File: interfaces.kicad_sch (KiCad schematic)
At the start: 10 parts, among them J13 JST_SH_1x4_SM04B-SRSS-TB-LF-SN, J14 JST_SH_1x4_SM04B-SRSS-TB-LF-SN, U7 MAX3051EKA

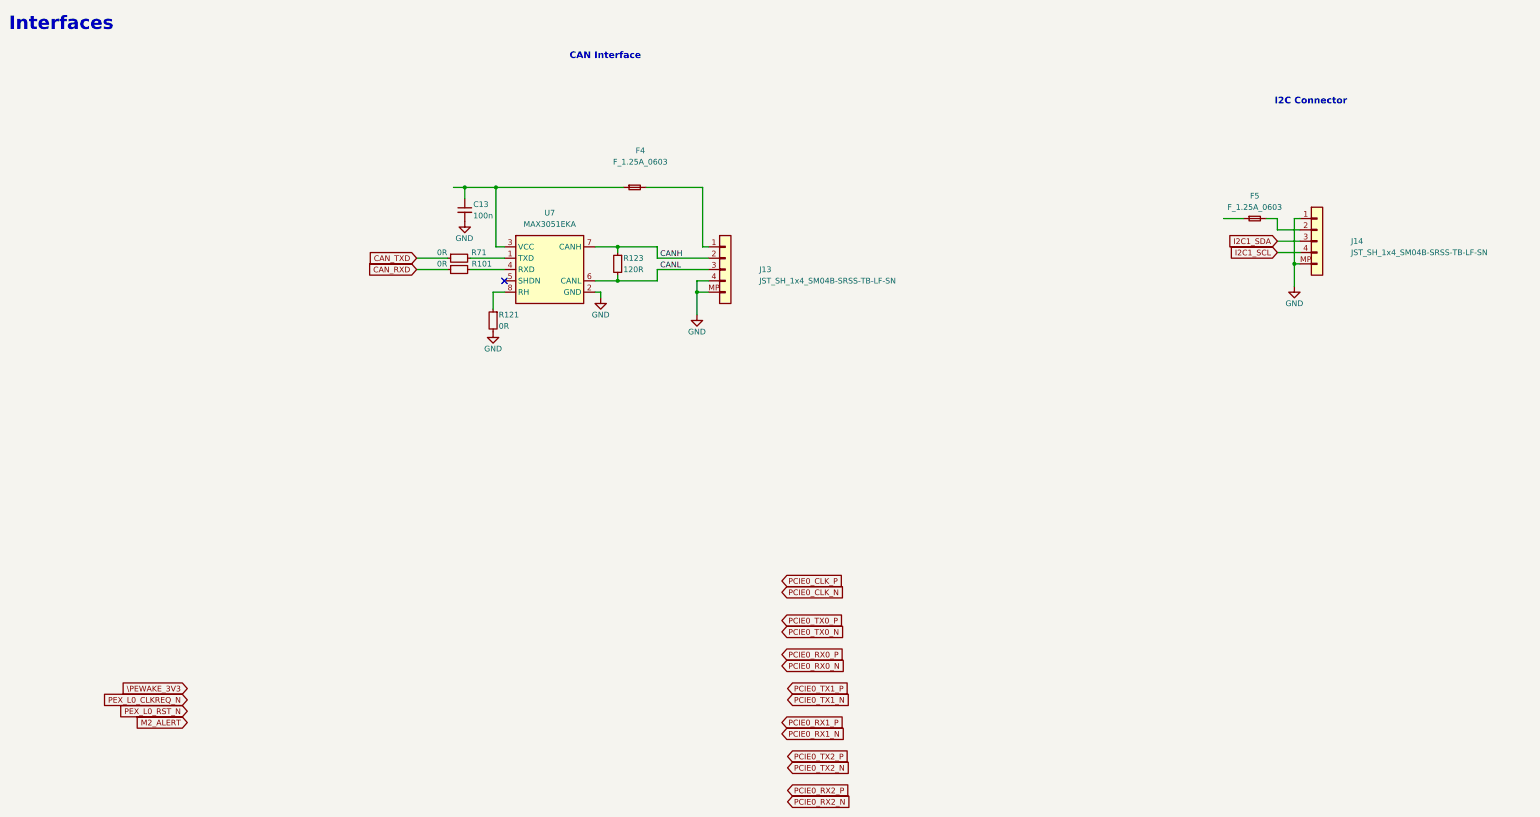
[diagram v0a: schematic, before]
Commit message: fix(schematic): remediate camera clocking, power sequencing, and ERC errors
- Connect Sony IMX219 master clocks (CAM0/1_MCLK) from SoM pins 116/122
- Connect independent PWDN hardware resets from SoM pins 114/120
- Isolate sensor I2C channels (CAM0/1_SCL/SDA) downstream of PCA9547
- Upgrade U11 digital core LDO to TLV75512PDBVR (500mA rating)
- Ground R132 to enable serial EEPROM write-protect
- Connect 3V3_SYS power rail to CAN transceiver U7 and fuse F5
- Eliminate dangling global labels across all sheets
- Configure 25 mil connection grid and achieve 0 ERC errors
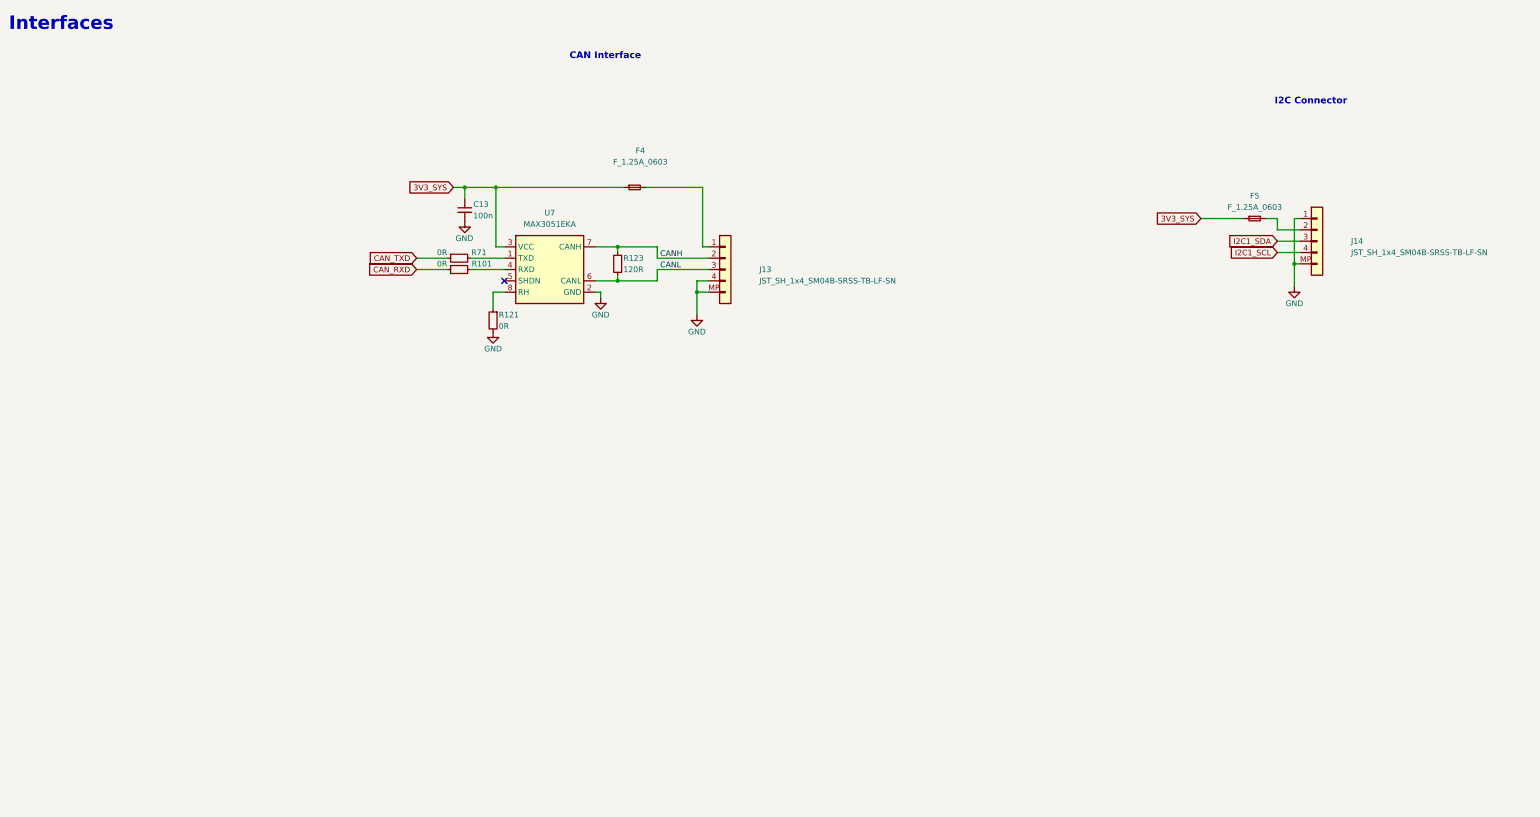
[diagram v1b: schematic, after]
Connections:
- net 3V3_SYS: now reaches C13.1, F4.1, U7.3 (VCC)
- net 3V3_SYS: now also F5.1

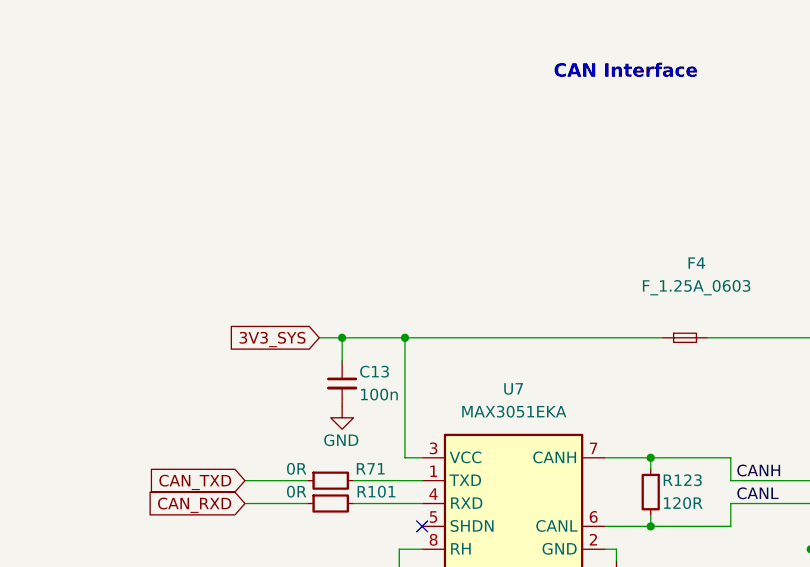
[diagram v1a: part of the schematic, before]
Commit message: fix(display, interfaces): connect U7 VCC to 3V3_SYS, change IC6 VCCA to 1V8_SYS, add display PWR_FLAGs
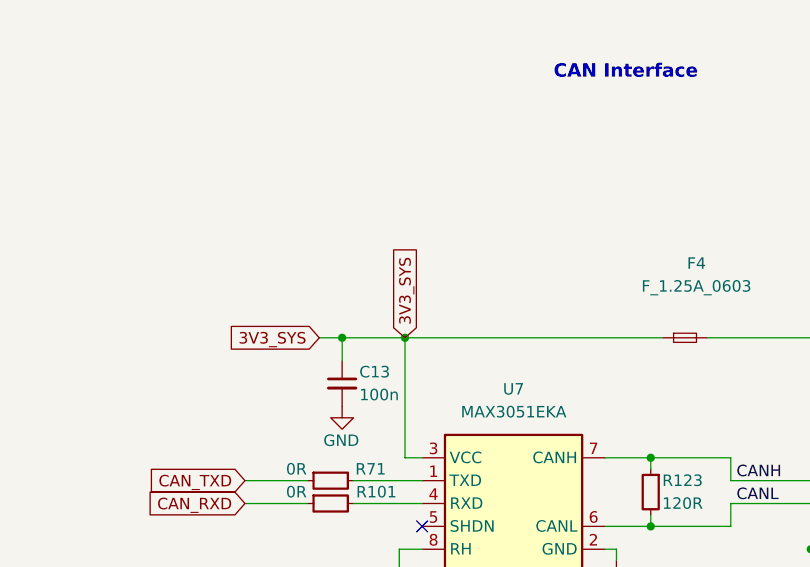
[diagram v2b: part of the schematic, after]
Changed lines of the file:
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@@
 		)
 	)
+	(global_label "3V3_SYS"
+		(shape input)
+		(at 126.365 57.785 90)
+		(fields_autoplaced yes)
+		(effects (font (size 1.27 1.27)) (justify left))
+	)
 )

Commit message: fix(schematic): resolve electrical omissions, CSI pairs, CAN power, DNP flags, and ERC stubs
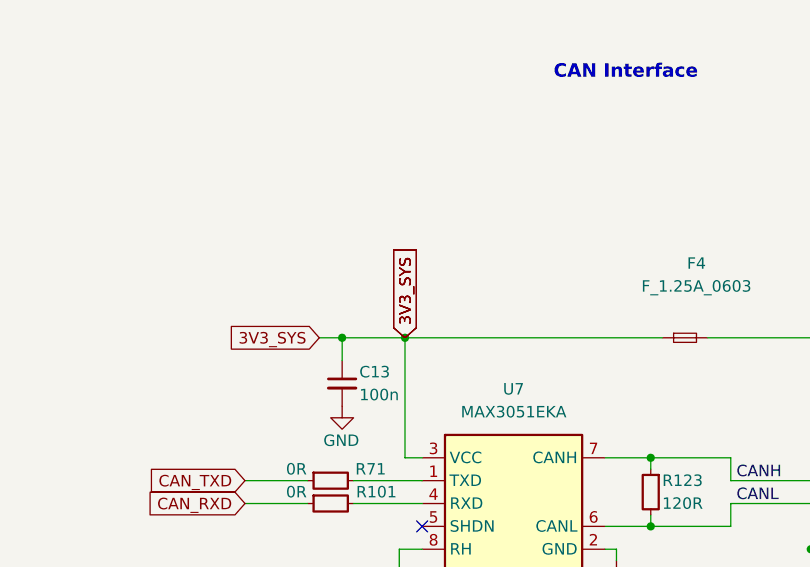
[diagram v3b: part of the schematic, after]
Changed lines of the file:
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@@
 		(color 0 0 0 0)
+	)
+	(global_label "3V3_SYS"
+		(shape input)
+		(at 126.365 57.785 90)
+		(fields_autoplaced yes)
+		(effects
+			(font
+				(size 1.27 1.27)
+			)
+			(justify left)
+		)
 	)
 	(junction

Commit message: feat(release): resolve all ERC/DRC/parity issues, complete 8-layer routing, and generate JLCPCB fab outputs
Resolve all schematic ERC violations, PCB DRC errors/warnings, schematic-to-PCB parity mismatches, and LCSC BOM/CPL fields, and package 8-layer Gerbers, drills, BOM, and CPL for JLCPCB manufacturing.

Co-Authored-By: CopperPilot <noreply@copperpilot.ai>
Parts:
- C13: LCSC (none) -> C1525
- F4, F5: LCSC (none) -> C150891
- J13, J14: LCSC (none) -> C160404
- R101, R121, R71: LCSC (none) -> C17168
- R123: LCSC (none) -> C25079
- U7: LCSC (none) -> C90741
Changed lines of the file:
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@@
+			)
+		)
+		(property "LCSC" "C160404"
+			(at 0 0 0)
+			(effects
+				(font
+					(size 1.27 1.27)
+				)
+				(hide yes)
 			)
 		)
@@
 			)
 		)
+		(property "LCSC" "C160404"
+			(at 0 0 0)
+			(effects
+				(font
+					(size 1.27 1.27)
+				)
+				(hide yes)
+			)
+		)
 		(pin "1"
 		)
@@
 			)
 		)
+		(property "LCSC" "C90741"
+			(at 0 0 0)
+			(effects
+				(font
+					(size 1.27 1.27)
+				)
+				(hide yes)
+			)
+		)
 		(pin "1"
 		)
@@
 			)
 		)
+		(property "LCSC" "C25079"
+			(at 0 0 0)
+			(effects
+				(font
+					(size 1.27 1.27)
+				)
+				(hide yes)
+			)
+		)
 		(pin "1"
 		)
@@
 			)
 		)
+		(property "LCSC" "C17168"
+			(at 0 0 0)
+			(effects
+				(font
+					(size 1.27 1.27)
+				)
+				(hide yes)
+			)
+		)
 		(pin "1"
 		)
@@
 				)
 				(justify left)
+			)
+		)
+		(property "LCSC" "C17168"
+			(at 0 0 0)
+			(effects
+				(font
+					(size 1.27 1.27)
+				)
+				(hide yes)
 			)
 		)
@@
 			)
 		)
+		(property "LCSC" "C150891"
+			(at 0 0 0)
+			(effects
+				(font
+					(size 1.27 1.27)
+				)
+				(hide yes)
+			)
+		)
 		(pin "1"
 		)
@@
 			)
 		)
+		(property "LCSC" "C150891"
+			(at 0 0 0)
+			(effects
+				(font
+					(size 1.27 1.27)
+				)
+				(hide yes)
+			)
+		)
 		(pin "1"
 		)
@@
 			)
 		)
+		(property "LCSC" "C17168"
+			(at 0 0 0)
+			(effects
+				(font
+					(size 1.27 1.27)
+				)
+				(hide yes)
+			)
+		)
 		(pin "1"
 		)
@@
 			)
 		)
+		(property "LCSC" "C1525"
+			(at 0 0 0)
+			(effects
+				(font
+					(size 1.27 1.27)
+				)
+				(hide yes)
+			)
+		)

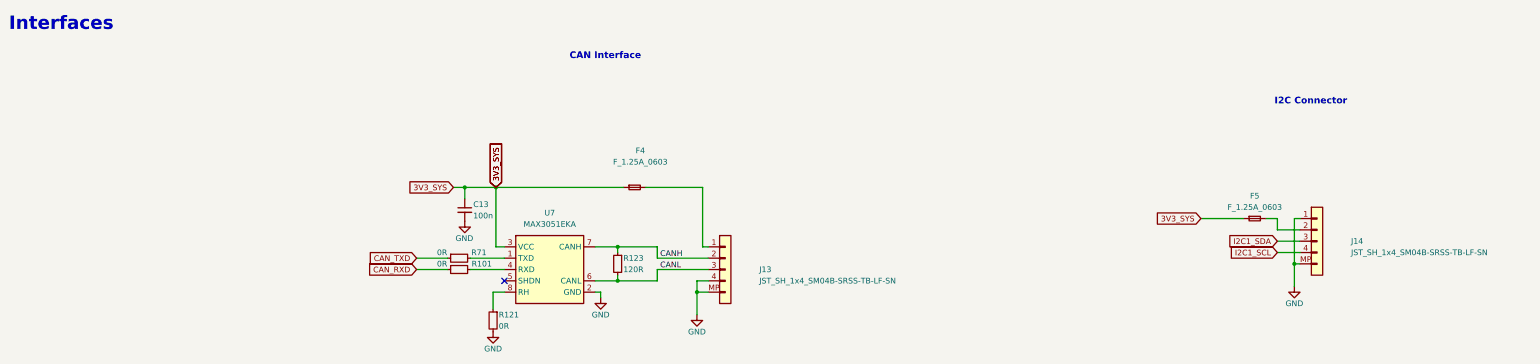
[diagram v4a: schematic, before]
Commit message: fix(sch): resolve label, wire, and property collisions on Root, ID Serial, and Interfaces sheets
Remove duplicate overlapping global labels on GEN0_SDA, GEN0_SCL, and 3V3_SYS, delete off-sheet stray artifacts, reposition R71/R101/C13 properties out of wire corridors, clear J14 MP pin number from vertical GND drop, and align hierarchical sheets to 1.27mm grid.

Co-Authored-By: CopperPilot <noreply@copperpilot.ai>
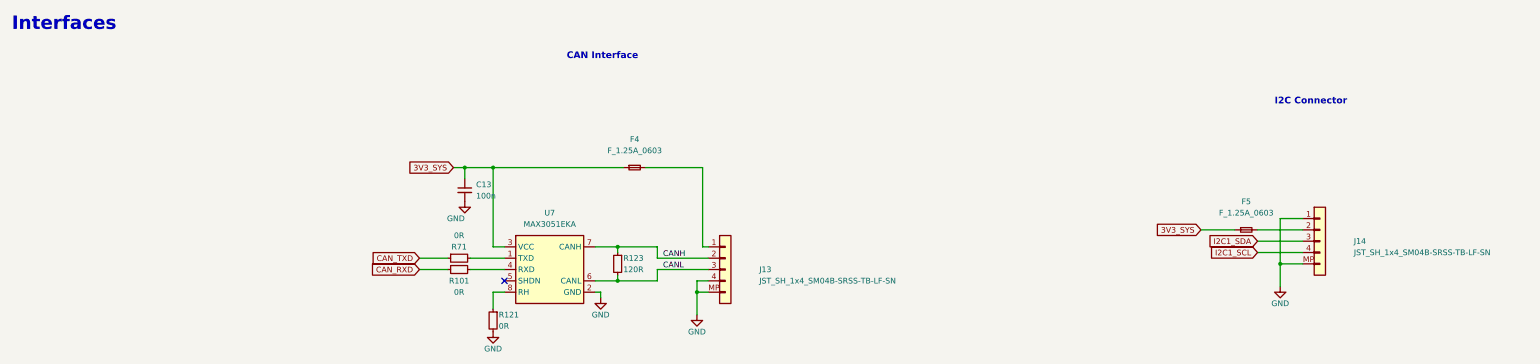
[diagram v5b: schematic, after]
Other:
- moved on the sheet: C13, F4, F5, J14

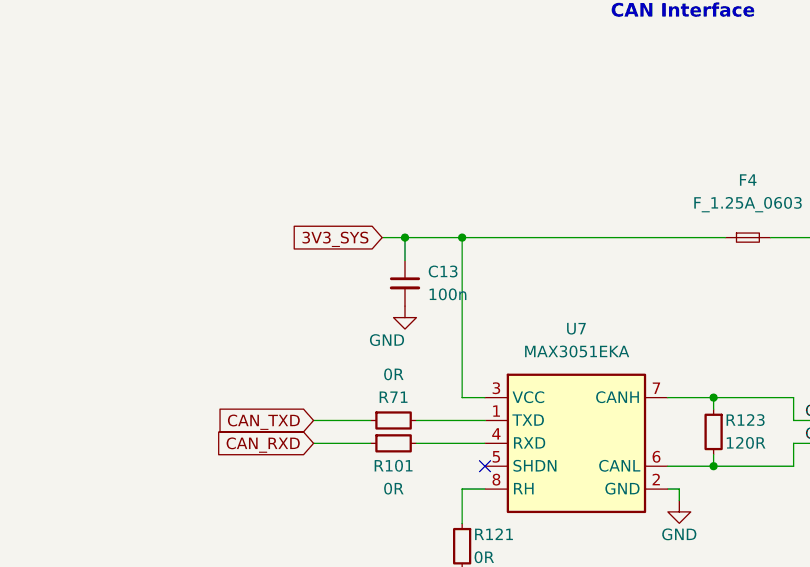
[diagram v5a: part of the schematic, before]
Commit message: fix(sch): resolve all symbol, label, property, and frame collisions on CSI sheet (Page 3)
Fix IMX219_30P symbol body height and SH pin placement, add wire stubs and outward justifications on all CAM_L/CAM_R/J15B/U4 global labels, rotate side GND symbols outward, unstack C95-C102/R140-R145/C91-C94/R13-R61 properties, shift U11 LDO block for clearance, and delete 24 stray junctions and 5 stray polylines.

Co-Authored-By: CopperPilot <noreply@copperpilot.ai>
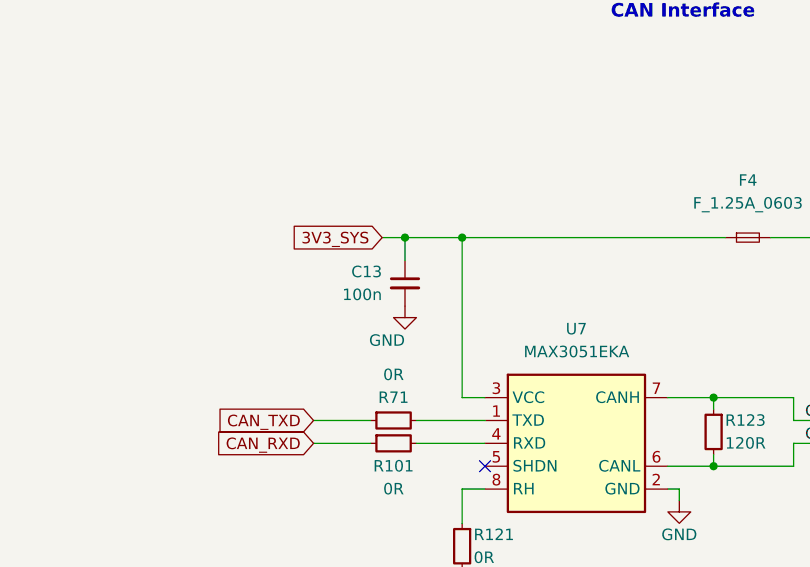
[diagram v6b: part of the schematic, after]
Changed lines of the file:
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@@
 		(dnp no)
 		(property "Reference" "C13"
-			(at 121.92 57.15 90)
+			(at 116.84 57.15 90)
 			(show_name no)
 			(do_not_autoplace no)
@@
 					(size 1.27 1.27)
 				)
-				(justify left)
+				(justify right)
 			)
 		)
@@
 		)
 		(property "Val" "100n"
-			(at 121.92 59.69 90)
+			(at 116.84 59.69 90)
 			(show_name no)
 			(do_not_autoplace no)
@@
 					(size 1.27 1.27)
 				)
-				(justify left)
+				(justify right)
 			)
 		)
